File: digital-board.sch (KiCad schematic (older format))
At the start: 241 parts, among them IC1 ATMEGA6450-A, J1 CONN_20X2, Q1 2N3904, Q2 2N3904, SW15 TACT_SWITCH, SW16 TACT_SWITCH, SW17 TACT_SWITCH, SW18 TACT_SWITCH, SW19 TACT_SWITCH, SW20 TACT_SWITCH, SW21 TACT_SWITCH, SW22 TACT_SWITCH, SW23 TACT_SWITCH, U1 DG419, U10 74LVC1G32, U11 74HC165, U12 74AC595, U13 74AC595, U14 74HC165, U15 74AC595, U16 74AC595, U2 74HC4067, U3 R-78E5.0-1.0, U4 74HC4067, U5 74LS573, U6 74LS573, U7 74LVC2G04, U8 74AC595, U9 74HC165, X1 MIDI OUT, X2 MIDI IN, X3 MIDI THRU

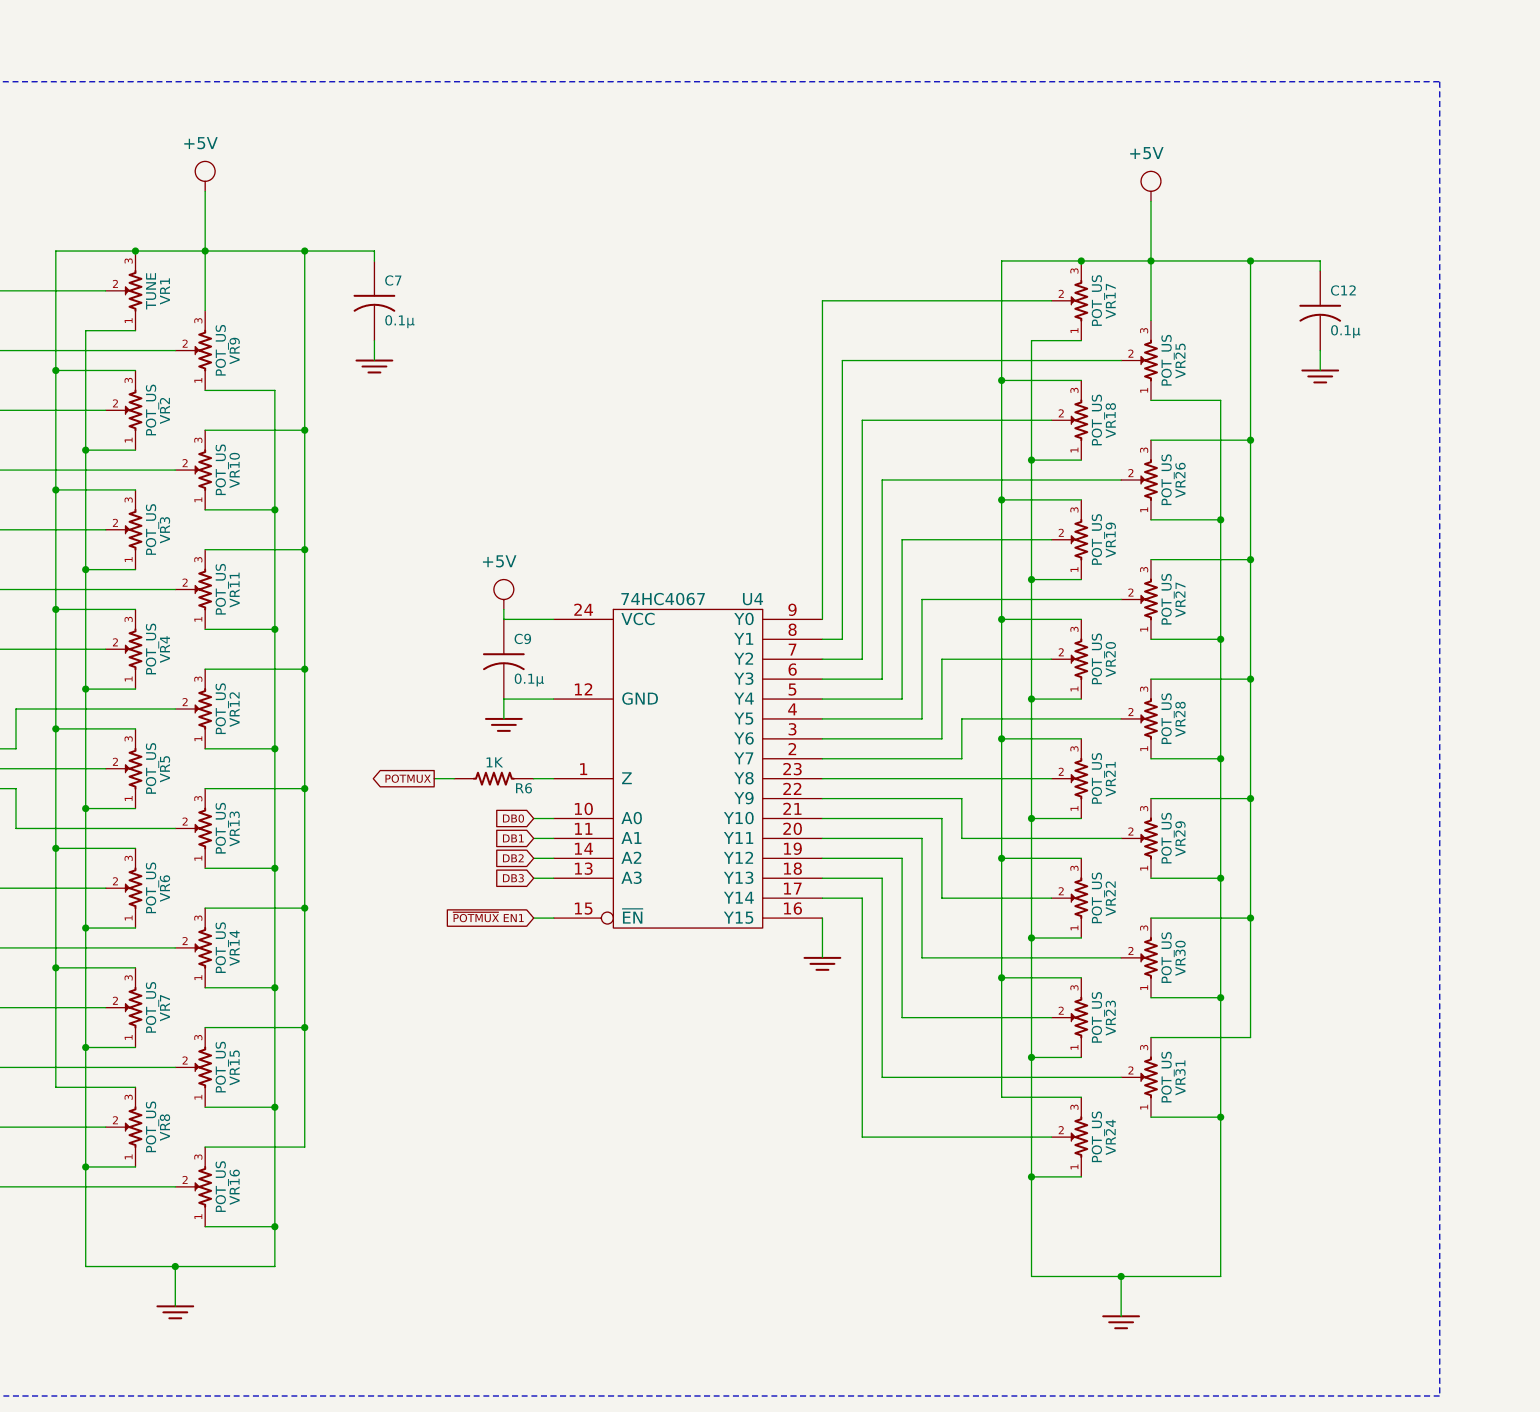
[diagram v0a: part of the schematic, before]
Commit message: all compoennts placed, time to start routing
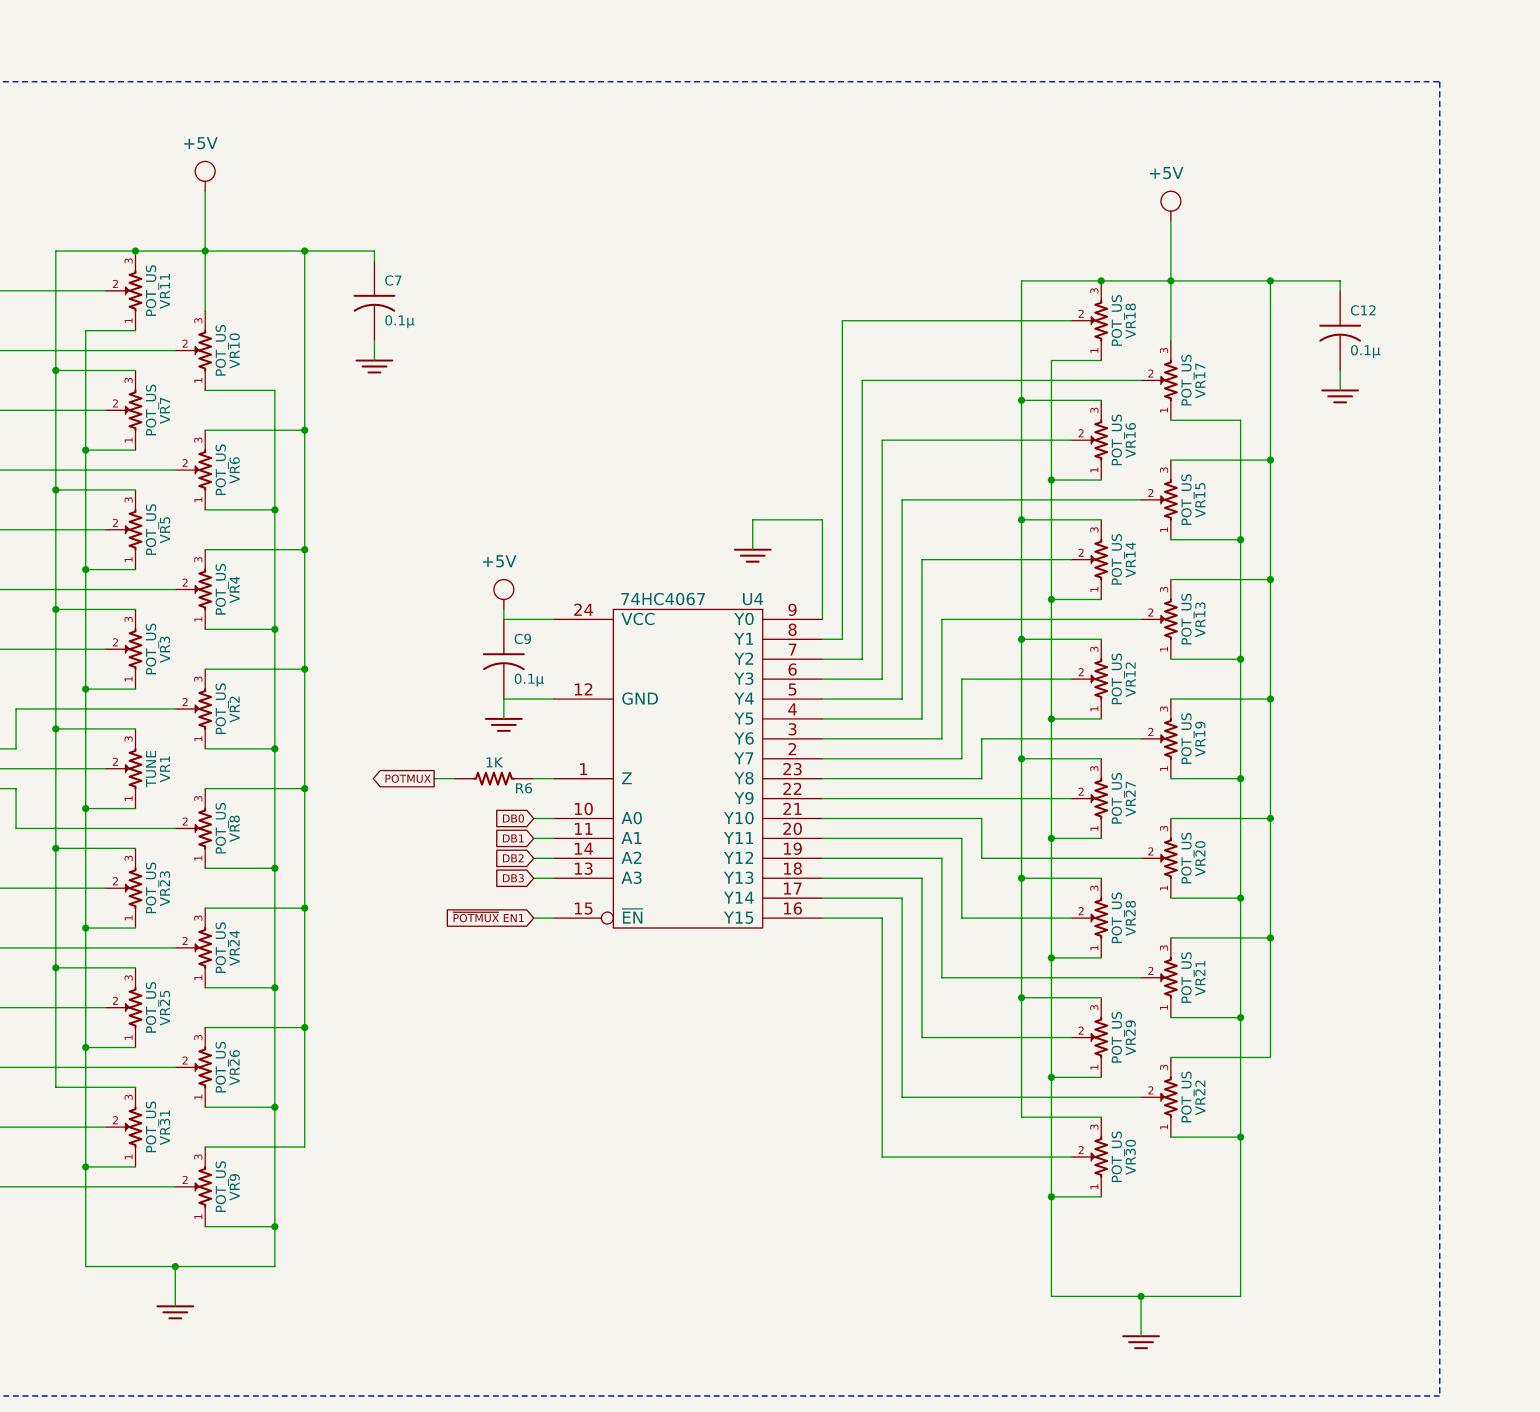
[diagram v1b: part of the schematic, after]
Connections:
- wire segments 945 -> 948
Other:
- moved on the sheet: C12, VR1, VR10, VR11, VR12, VR13, VR14, VR15, VR16, VR17, VR18, VR19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

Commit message: about to start routing
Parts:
- VR10: value POT_US -> VCO1 MIX
- VR11: value POT_US -> VCO2 MIX
- VR12: value POT_US -> NOISE
- VR13: value POT_US -> FIL LFO
- VR14: value POT_US -> FIL VCO2
- VR15: value POT_US -> KEY TRACK
- VR16: value POT_US -> FIL EG2
- VR17: value POT_US -> CUTOFF
- VR18: value POT_US -> RES
- VR19, VR27: value POT_US -> ATTACK
- VR2: value POT_US -> VCO1 PW
- VR20, VR28: value POT_US -> DECAY
- VR21, VR29: value POT_US -> SUSTAIN
- VR22, VR30: value POT_US -> RELEASE
- VR23: value POT_US -> LFO RATE
- VR24: value POT_US -> ARP RATE
- VR25: value POT_US -> GLIDE
- VR26: value POT_US -> AMP LFO
- VR3: value POT_US -> PWM EG2
- VR31: value POT_US -> VOLUME
- VR4: value POT_US -> PWM LFO
- VR5: value POT_US -> PITCH LFO
- VR6: value POT_US -> PITCH VCO2
- VR7: value POT_US -> PITCH EG2
- VR8: value POT_US -> FINE
- VR9: value POT_US -> VCO2 PW
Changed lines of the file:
@@
 P 6300 17800
 F 0 "VR2" H 6300 17650 50  0000 C CNN
-F 1 "POT_US" H 6300 17720 50  0000 C CNN
+F 1 "VCO1 PW" H 6300 17720 50  0000 C CNN
 F 2 "" H 6300 17800 60  0000 C CNN
 F 3 "" H 6300 17800 60  0000 C CNN
@@
 P 6300 20200
 F 0 "VR9" H 6300 20050 50  0000 C CNN
-F 1 "POT_US" H 6300 20120 50  0000 C CNN
+F 1 "VCO2 PW" H 6300 20120 50  0000 C CNN
 F 2 "" H 6300 20200 60  0000 C CNN
 F 3 "" H 6300 20200 60  0000 C CNN
@@
 P 6300 16000
 F 0 "VR10" H 6300 15850 50  0000 C CNN
-F 1 "POT_US" H 6300 15920 50  0000 C CNN
+F 1 "VCO1 MIX" H 6300 15920 50  0000 C CNN
 F 2 "" H 6300 16000 60  0000 C CNN
 F 3 "" H 6300 16000 60  0000 C CNN
@@
 P 5950 17500
 F 0 "VR3" H 5950 17350 50  0000 C CNN
-F 1 "POT_US" H 5950 17420 50  0000 C CNN
+F 1 "PWM EG2" H 5950 17420 50  0000 C CNN
 F 2 "" H 5950 17500 60  0000 C CNN
 F 3 "" H 5950 17500 60  0000 C CNN
@@
 P 5950 15700
 F 0 "VR11" H 5950 15550 50  0000 C CNN
-F 1 "POT_US" H 5950 15620 50  0000 C CNN
+F 1 "VCO2 MIX" H 5950 15620 50  0000 C CNN
 F 2 "" H 5950 15700 60  0000 C CNN
 F 3 "" H 5950 15700 60  0000 C CNN
@@
 P 6300 17200
 F 0 "VR4" H 6300 17050 50  0000 C CNN
-F 1 "POT_US" H 6300 17120 50  0000 C CNN
+F 1 "PWM LFO" H 6300 17120 50  0000 C CNN
 F 2 "" H 6300 17200 60  0000 C CNN
 F 3 "" H 6300 17200 60  0000 C CNN
@@
 P 10800 17650
 F 0 "VR12" H 10800 17500 50  0000 C CNN
-F 1 "POT_US" H 10800 17570 50  0000 C CNN
+F 1 "NOISE" H 10800 17570 50  0000 C CNN
 F 2 "" H 10800 17650 60  0000 C CNN
 F 3 "" H 10800 17650 60  0000 C CNN
@@
 P 5950 16900
 F 0 "VR5" H 5950 16750 50  0000 C CNN
-F 1 "POT_US" H 5950 16820 50  0000 C CNN
+F 1 "PITCH LFO" H 5950 16820 50  0000 C CNN
 F 2 "" H 5950 16900 60  0000 C CNN
 F 3 "" H 5950 16900 60  0000 C CNN
@@
 P 11150 17350
 F 0 "VR13" H 11150 17200 50  0000 C CNN
-F 1 "POT_US" H 11150 17270 50  0000 C CNN
+F 1 "FIL LFO" H 11150 17270 50  0000 C CNN
 F 2 "" H 11150 17350 60  0000 C CNN
 F 3 "" H 11150 17350 60  0000 C CNN
@@
 P 6300 16600
 F 0 "VR6" H 6300 16450 50  0000 C CNN
-F 1 "POT_US" H 6300 16520 50  0000 C CNN
+F 1 "PITCH VCO2" H 6300 16520 50  0000 C CNN
 F 2 "" H 6300 16600 60  0000 C CNN
 F 3 "" H 6300 16600 60  0000 C CNN
@@
 P 10800 17050
 F 0 "VR14" H 10800 16900 50  0000 C CNN
-F 1 "POT_US" H 10800 16970 50  0000 C CNN
+F 1 "FIL VCO2" H 10800 16970 50  0000 C CNN
 F 2 "" H 10800 17050 60  0000 C CNN
 F 3 "" H 10800 17050 60  0000 C CNN
@@
 P 5950 16300
 F 0 "VR7" H 5950 16150 50  0000 C CNN
-F 1 "POT_US" H 5950 16220 50  0000 C CNN
+F 1 "PITCH EG2" H 5950 16220 50  0000 C CNN
 F 2 "" H 5950 16300 60  0000 C CNN
 F 3 "" H 5950 16300 60  0000 C CNN
@@
 P 11150 16750
 F 0 "VR15" H 11150 16600 50  0000 C CNN
-F 1 "POT_US" H 11150 16670 50  0000 C CNN
+F 1 "KEY TRACK" H 11150 16670 50  0000 C CNN
 F 2 "" H 11150 16750 60  0000 C CNN
 F 3 "" H 11150 16750 60  0000 C CNN
@@
 U 1 1 5499E3FE
 P 6300 18400
-F 0 "VR8" H 6300 18250 50  0000 C CNN
-F 1 "POT_US" H 6300 18320 50  0000 C CNN
+F 0 "VR8" V 6250 18250 50  0000 C CNN
+F 1 "FINE" V 6350 18250 50  0000 C CNN
 F 2 "" H 6300 18400 60  0000 C CNN
 F 3 "" H 6300 18400 60  0000 C CNN
@@
 P 10800 16450
 F 0 "VR16" H 10800 16300 50  0000 C CNN
-F 1 "POT_US" H 10800 16370 50  0000 C CNN
+F 1 "FIL EG2" H 10800 16370 50  0000 C CNN
 F 2 "" H 10800 16450 60  0000 C CNN
 F 3 "" H 10800 16450 60  0000 C CNN
@@
 P 11150 16150
 F 0 "VR17" H 11150 16000 50  0000 C CNN
-F 1 "POT_US" H 11150 16070 50  0000 C CNN
+F 1 "CUTOFF" H 11150 16070 50  0000 C CNN
 F 2 "" H 11150 16150 60  0000 C CNN
 F 3 "" H 11150 16150 60  0000 C CNN
@@
 P 10800 15850
 F 0 "VR18" H 10800 15700 50  0000 C CNN
-F 1 "POT_US" H 10800 15770 50  0000 C CNN
+F 1 "RES" H 10800 15770 50  0000 C CNN
 F 2 "" H 10800 15850 60  0000 C CNN
 F 3 "" H 10800 15850 60  0000 C CNN
@@
 P 5950 19300
 F 0 "VR25" H 5950 19150 50  0000 C CNN
-F 1 "POT_US" H 5950 19220 50  0000 C CNN
+F 1 "GLIDE" H 5950 19220 50  0000 C CNN
 F 2 "" H 5950 19300 60  0000 C CNN
 F 3 "" H 5950 19300 60  0000 C CNN
@@
 P 6300 19600
 F 0 "VR26" H 6300 19450 50  0000 C CNN
-F 1 "POT_US" H 6300 19520 50  0000 C CNN
+F 1 "AMP LFO" H 6300 19520 50  0000 C CNN
 F 2 "" H 6300 19600 60  0000 C CNN
 F 3 "" H 6300 19600 60  0000 C CNN
@@
 P 11150 17950
 F 0 "VR19" H 11150 17800 50  0000 C CNN
-F 1 "POT_US" H 11150 17870 50  0000 C CNN
+F 1 "ATTACK" H 11150 17870 50  0000 C CNN
 F 2 "" H 11150 17950 60  0000 C CNN
 F 3 "" H 11150 17950 60  0000 C CNN
@@
 P 10800 18250
 F 0 "VR27" H 10800 18100 50  0000 C CNN
-F 1 "POT_US" H 10800 18170 50  0000 C CNN
+F 1 "ATTACK" H 10800 18170 50  0000 C CNN
 F 2 "" H 10800 18250 60  0000 C CNN
 F 3 "" H 10800 18250 60  0000 C CNN
@@
 P 11150 18550
 F 0 "VR20" H 11150 18400 50  0000 C CNN
-F 1 "POT_US" H 11150 18470 50  0000 C CNN
+F 1 "DECAY" H 11150 18470 50  0000 C CNN
 F 2 "" H 11150 18550 60  0000 C CNN
 F 3 "" H 11150 18550 60  0000 C CNN
@@
 P 10800 18850
 F 0 "VR28" H 10800 18700 50  0000 C CNN
-F 1 "POT_US" H 10800 18770 50  0000 C CNN
+F 1 "DECAY" H 10800 18770 50  0000 C CNN
 F 2 "" H 10800 18850 60  0000 C CNN
 F 3 "" H 10800 18850 60  0000 C CNN
@@
 P 11150 19150
 F 0 "VR21" H 11150 19000 50  0000 C CNN
-F 1 "POT_US" H 11150 19070 50  0000 C CNN
+F 1 "SUSTAIN" H 11150 19070 50  0000 C CNN
 F 2 "" H 11150 19150 60  0000 C CNN
 F 3 "" H 11150 19150 60  0000 C CNN
@@
 P 10800 19450
 F 0 "VR29" H 10800 19300 50  0000 C CNN
-F 1 "POT_US" H 10800 19370 50  0000 C CNN
+F 1 "SUSTAIN" H 10800 19370 50  0000 C CNN
 F 2 "" H 10800 19450 60  0000 C CNN
 F 3 "" H 10800 19450 60  0000 C CNN
@@
 P 11150 19750
 F 0 "VR22" H 11150 19600 50  0000 C CNN
-F 1 "POT_US" H 11150 19670 50  0000 C CNN
+F 1 "RELEASE" H 11150 19670 50  0000 C CNN
 F 2 "" H 11150 19750 60  0000 C CNN
 F 3 "" H 11150 19750 60  0000 C CNN
@@
 P 10800 20050
 F 0 "VR30" H 10800 19900 50  0000 C CNN
-F 1 "POT_US" H 10800 19970 50  0000 C CNN
+F 1 "RELEASE" H 10800 19970 50  0000 C CNN
 F 2 "" H 10800 20050 60  0000 C CNN
 F 3 "" H 10800 20050 60  0000 C CNN
@@
 P 5950 18700
 F 0 "VR23" H 5950 18550 50  0000 C CNN
-F 1 "POT_US" H 5950 18620 50  0000 C CNN
+F 1 "LFO RATE" H 5950 18620 50  0000 C CNN
 F 2 "" H 5950 18700 60  0000 C CNN
 F 3 "" H 5950 18700 60  0000 C CNN
@@
 P 5950 19900
 F 0 "VR31" H 5950 19750 50  0000 C CNN
-F 1 "POT_US" H 5950 19820 50  0000 C CNN
+F 1 "VOLUME" H 5950 19820 50  0000 C CNN
 F 2 "" H 5950 19900 60  0000 C CNN
 F 3 "" H 5950 19900 60  0000 C CNN
@@
 P 6300 19000
 F 0 "VR24" H 6300 18850 50  0000 C CNN
-F 1 "POT_US" H 6300 18920 50  0000 C CNN
+F 1 "ARP RATE" H 6300 18920 50  0000 C CNN
 F 2 "" H 6300 19000 60  0000 C CNN
 F 3 "" H 6300 19000 60  0000 C CNN

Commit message: started routing with Kicad p&s router
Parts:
- removed TP1, TP2, TP3, TP4, TP5, TP6, TP7, TP8: CONN_1, symbol CONN_1
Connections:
- wire segments 948 -> 933
- no-connect marks 25 -> 33
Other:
- moved on the sheet: LED17, LED18, LED19, LED20, R61, R62, R64, R66

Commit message: routing
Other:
- note added: "Changed from \n+12V to +5V\nneed to test this!"
- moved on the sheet: ISW12A, ISW13A, LED11, LED12, R55, R59, R63, R67, R69, SW20, VR1, VR8
